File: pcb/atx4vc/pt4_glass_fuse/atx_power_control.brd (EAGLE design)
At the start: 86 x 70 mm, 62 parts, among them IC2 REG1117, IC3 STM32F042F4, IC4 MY_7905DT, J1 ATX24RH, SW1 324_SW, SW2 324_SW, SW3 324_SW, SW4 324_SW, SW5 324_SW, SW7 324_SW, U1 USBC_16P, U2 USBC_16P

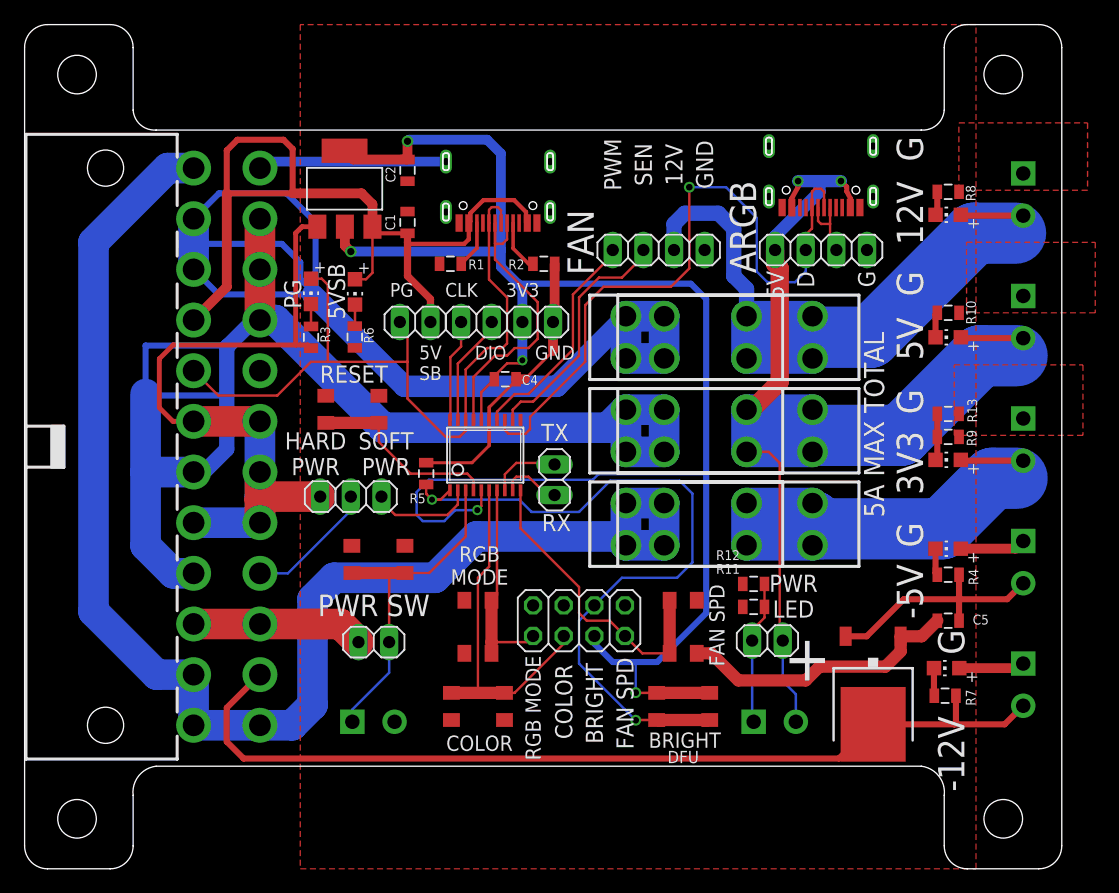
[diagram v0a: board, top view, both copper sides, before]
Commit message: updated PCB to use car fuse holder
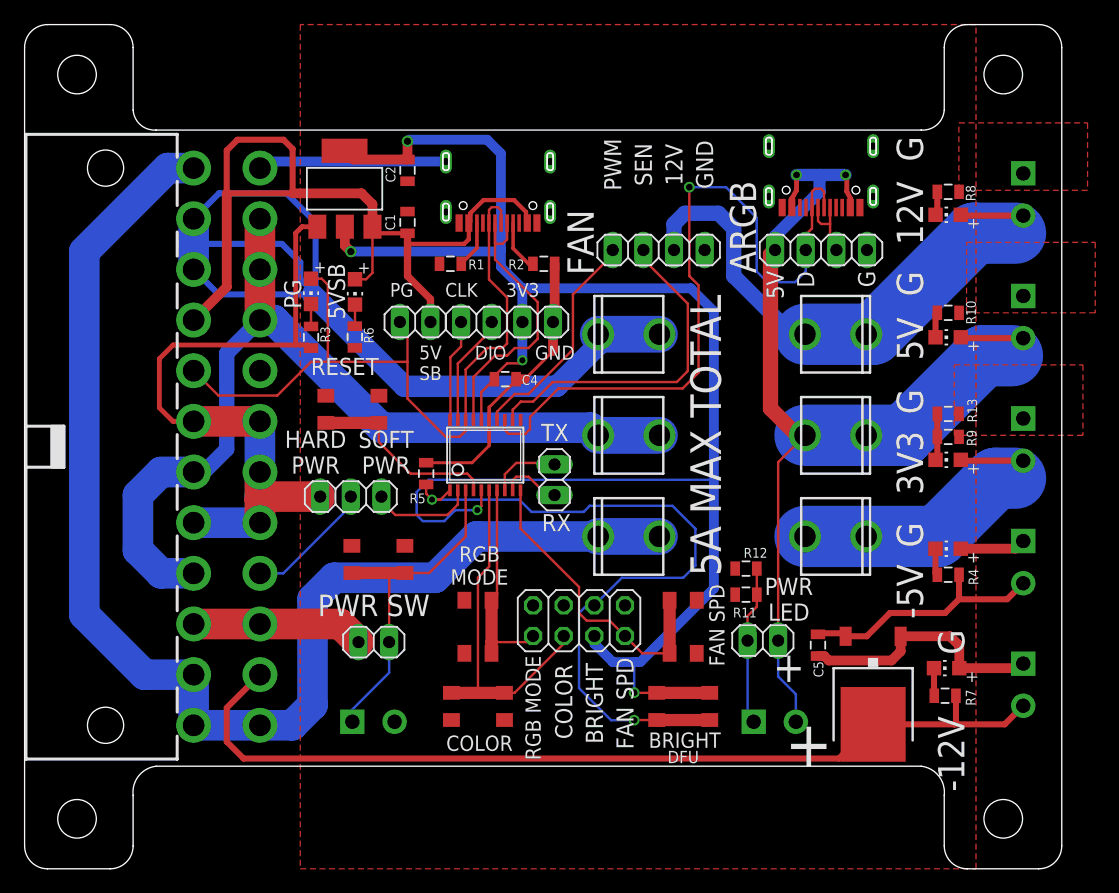
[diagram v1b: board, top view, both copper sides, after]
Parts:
- removed U$4, U$6, U$9: FUSE_HOLDER, atx_power_control:FUSE_HOLDER_MINI_ONLY
- removed U$5, U$7, U$8: CAR_FUSE_HOLDER3IN1, atx_power_control:FUSE_HOLDER_3IN1
- added F1, F2, F3: FUSEX20MM, atx_power_control:FUSE_5MM
- moved C5 11.0 mm to (65.8, 18.5), turned to 90 degrees
- moved R12 1.42 mm to (59.8, 24.9)
- moved R11 1.20 mm to (59.8, 22.7)
- moved JP1 0.38 mm to (61.2, 18.9)
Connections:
- removed net N$15: J6.2, JP2.3, LED5.A, U$4.B0, U$4.B1, U$5.B0, U$5.B1
- new net N$19: F3.3, F3.4, J2.2, LED6.A
- net N$10: now also F1.1, F1.2; no longer U$8.A0, U$8.A1, U$9.A0, U$9.A1
- net N$14: now also F3.1, F3.2; no longer U$6.A0, U$6.A1, U$7.A0, U$7.A1
- net N$16: now also F2.1, F2.2, J6.2, JP2.3, LED5.A; no longer J2.2, LED6.A, U$6.B0, U$6.B1, U$7.B0, U$7.B1
- net N$21: now also F2.3, F2.4; no longer U$4.A0, U$4.A1, U$5.A0, U$5.A1
- net N$30: now also F1.3, F1.4; no longer U$8.B0, U$8.B1, U$9.B0, U$9.B1
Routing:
- net N$15: track 65.9 -> 0.00 mm
- net N$10: track 111.3 -> 76.3 mm
- net N$19: track 0.00 -> 26.4 mm
- net N$30: track 106.4 -> 86.8 mm
- net N$21: track 90.7 -> 80.0 mm
- net N$14: track 117.2 -> 107.6 mm
- net GND: track 153.6 -> 145.5 mm
- net N$6: track 20.3 -> 28.2 mm
- net N$35: track 57.3 -> 60.6 mm
- net N$16: track 50.1 -> 47.7 mm
- net N$17: track 11.9 -> 13.2 mm
- net BUTTON2: track 60.3 -> 59.0 mm
- net N$11: track 20.4 -> 21.0 mm
